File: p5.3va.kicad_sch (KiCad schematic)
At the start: 22 parts, among them U10 LT3045xDD, U19 LT3015EDDPBF

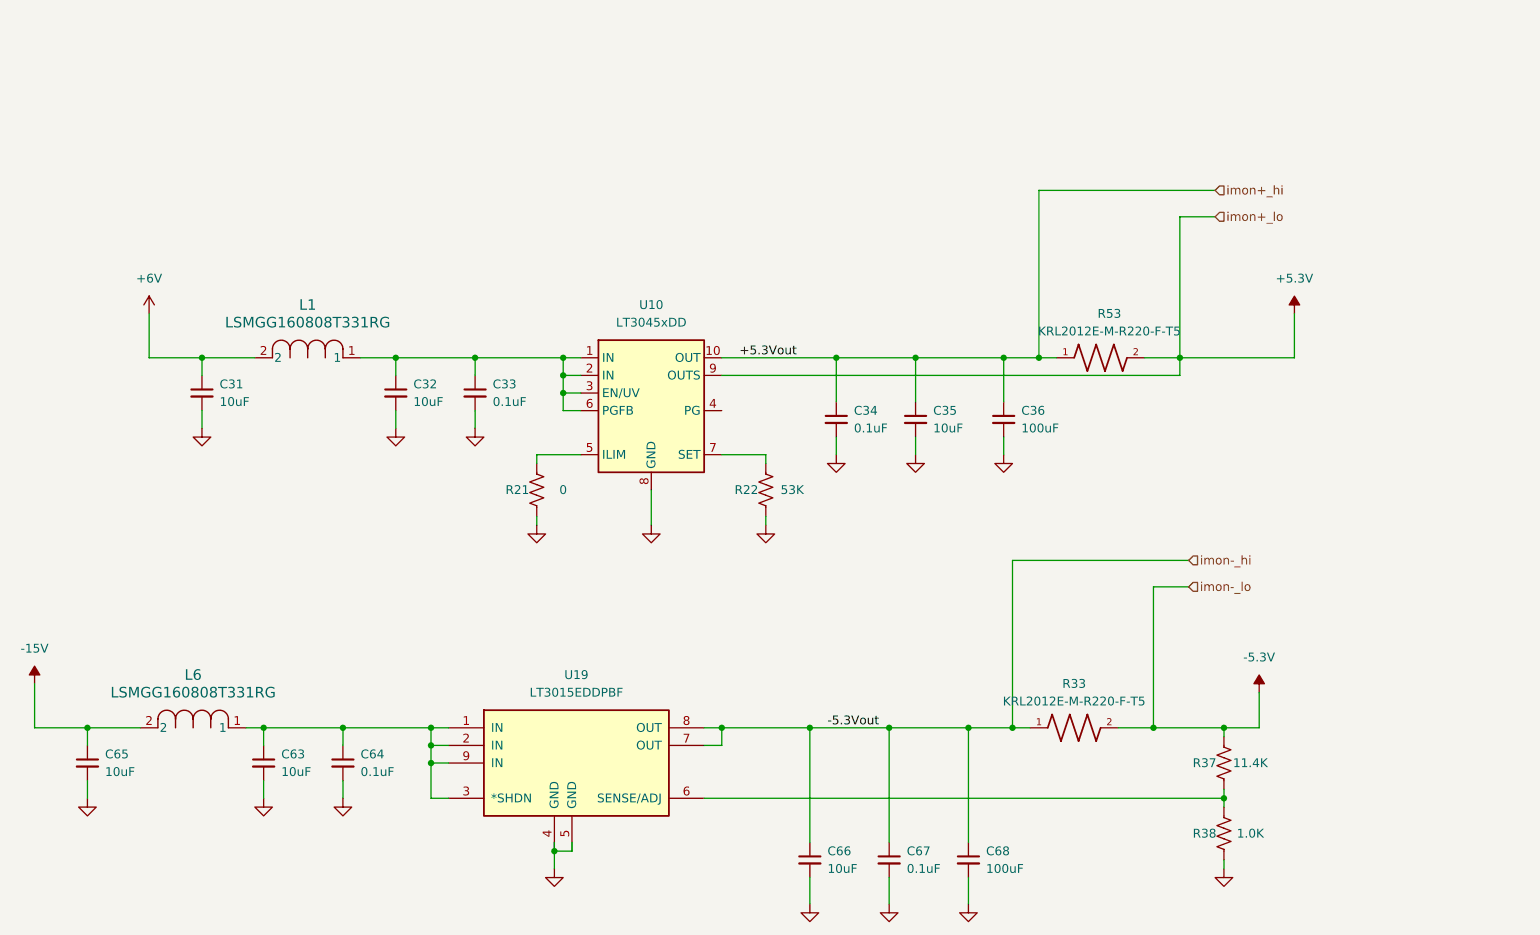
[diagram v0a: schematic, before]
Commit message: Add all 4 channels
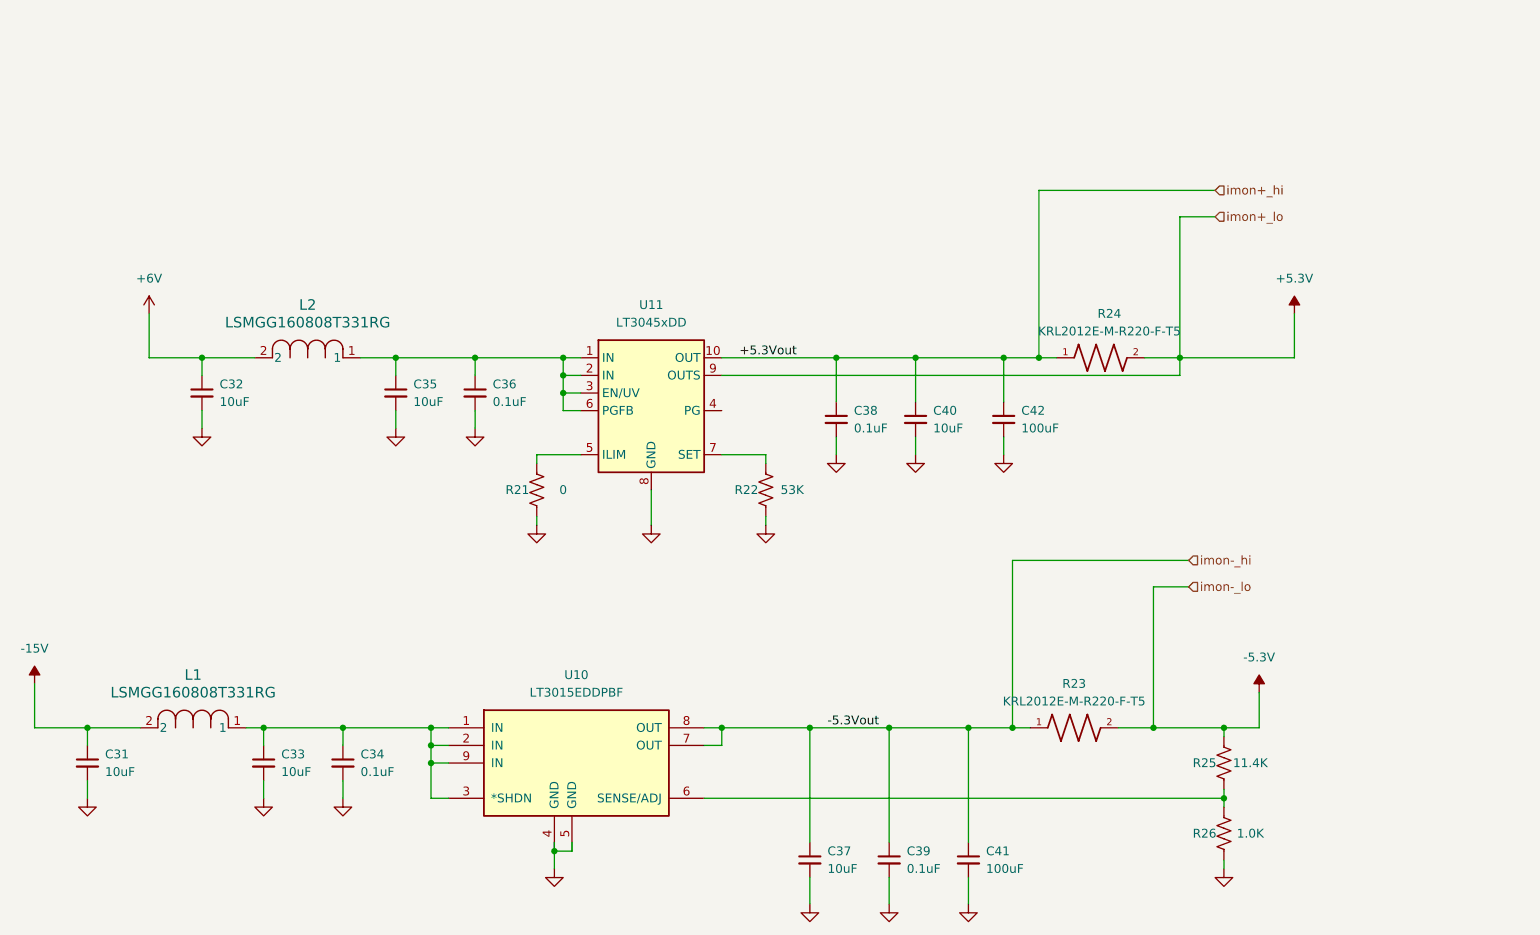
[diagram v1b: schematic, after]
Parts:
- renumbered C65 to C31, C31 to C32, C63 to C33, C64 to C34, C32 to C35, C33 to C36, C66 to C37, C34 to C38, C67 to C39, C35 to C40, C68 to C41, C36 to C42, L6 to L1, L1 to L2, R33 to R23, R53 to R24, R37 to R25, R38 to R26, U19 to U10, U10 to U11

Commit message: Start routing
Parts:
- renumbered C31 to C16, C32 to C17, C33 to C18, C34 to C19, C35 to C20, C36 to C21, C37 to C22, C38 to C23, C39 to C24, C40 to C25, C41 to C26, C42 to C27, R21 to R11, R22 to R12, R23 to R13, R24 to R14, R25 to R15, R26 to R16, U10 to U6, U11 to U7
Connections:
- net +6V renamed +15V
- no-connect marks 0 -> 2
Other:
- note added: "Expected Iout = 9mA*4 + 5mA*4 = 56mA Pd = 56mA * 9.7v = 0.54W deltaT ~ 25 C"
- moved on the sheet: C17, C20, C21, C23, C25, C27, L2, R11, R12, R14, U7

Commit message: Finished layout
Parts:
- added TP3, TP4: ${SHORT_NET_NAME(1)}, TestPoint:TestPoint_THTPad_D2.0mm_Drill1.0mm, symbol Connector:TestPoint
- C16, C17, C18, C20, C22, C25: Cost (none) -> .04; MFG (none) -> Samsung; MFG_PN (none) -> CL10A106MA8NRNC
- C19, C21, C23, C24: Cost (none) -> .01; MFG (none) -> Taiyo Yuden; MFG_PN (none) -> TMK105BJ104KV-F
- C26, C27: Cost (none) -> 0.22; MFG (none) -> Murata; MFG_PN (none) -> GRM31CR61A107MEA8L
- L1, L2: Cost (none) -> .01; MFG (none) -> Taiyo Yuden; MFG_PN (none) -> LSMGG160808T331RG
- R11: Cost (none) -> 0.01; MFG (none) -> Panasonic; MFG_PN (none) -> ERJ-2GE0R00X
- R12: value 53K -> 53.6K; Cost (none) -> 0.01; MFG (none) -> Panasonic; MFG_PN (none) -> ERJ-2RKF5362X
- R13, R14: value KRL2012E-M-R220-F-T5 -> 0.22; Cost (none) -> 0.38; MFG (none) -> Susumu; MFG_PN (none) -> KRL2012E-M-R220-F-T5
- R15: value 11.4K -> 11.5K; Cost (none) -> 0.01; MFG (none) -> Panasonic; MFG_PN (none) -> ERJ-2RKF1152X
- R16: Cost (none) -> 0.01; MFG (none) -> Panasonic; MFG_PN (none) -> ERJ-2RKF1001X
- U6: Cost (none) -> 5.79; MFG (none) -> Analog Devices; MFG_PN (none) -> LT3015EDD#PBF
- U7: Cost (none) -> 6.06; MFG (none) -> Analog Devices; MFG_PN (none) -> LT3045EDD#TRPBF
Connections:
- net +5.3V: now also TP3.1
- net -5.3V: now also TP4.1
- net +15Vin: now reaches C20.1, C21.1, L2.1, U7.1 (IN), U7.2 (IN), U7.3 (EN/UV), U7.6 (PGFB)
- net -15Vin: now reaches C18.1, C19.1, L1.1, U6.1 (IN), U6.2 (IN), U6.3 (*SHDN), U6.9 (IN)
